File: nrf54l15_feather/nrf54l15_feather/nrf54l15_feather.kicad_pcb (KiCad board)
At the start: 4 copper layers, 66 x 25.4 mm, 63 parts, among them CN1 503480-1400, IC1 AEM10330-QFN, J1 TYPE-C-31-M-12, J3 FTSH-105-01-L-DV-K, U2 nPM1300-QEXX, U4 S2B-PH-K-S-GW, U5 S2B-PH-K-S-GW, U6 nRF54L15-QFXX, X1 XL7EL89CKI-111YLC-32M

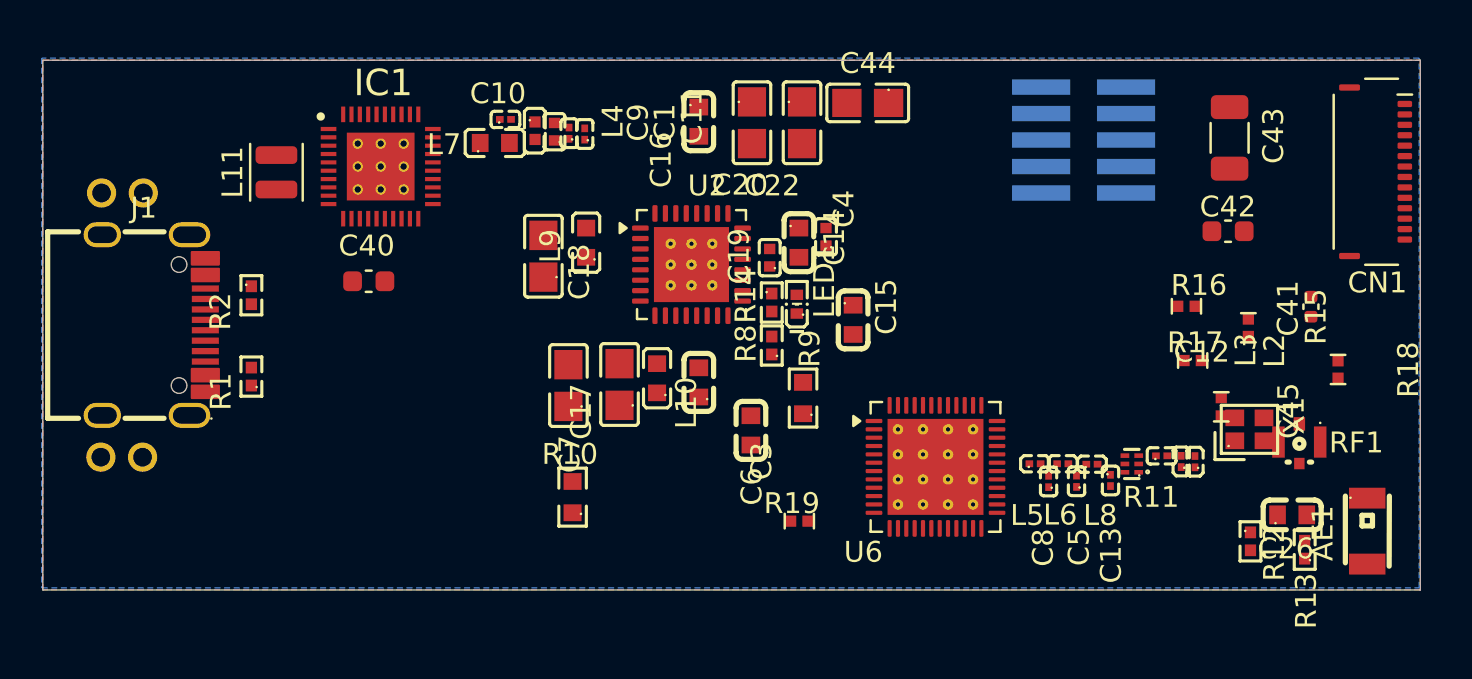
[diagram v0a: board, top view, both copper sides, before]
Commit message: Update the nRF54L15 feather and add the feather sens1 and pouch gateway designs.
Co-authored-by: Cursor <cursoragent@cursor.com>
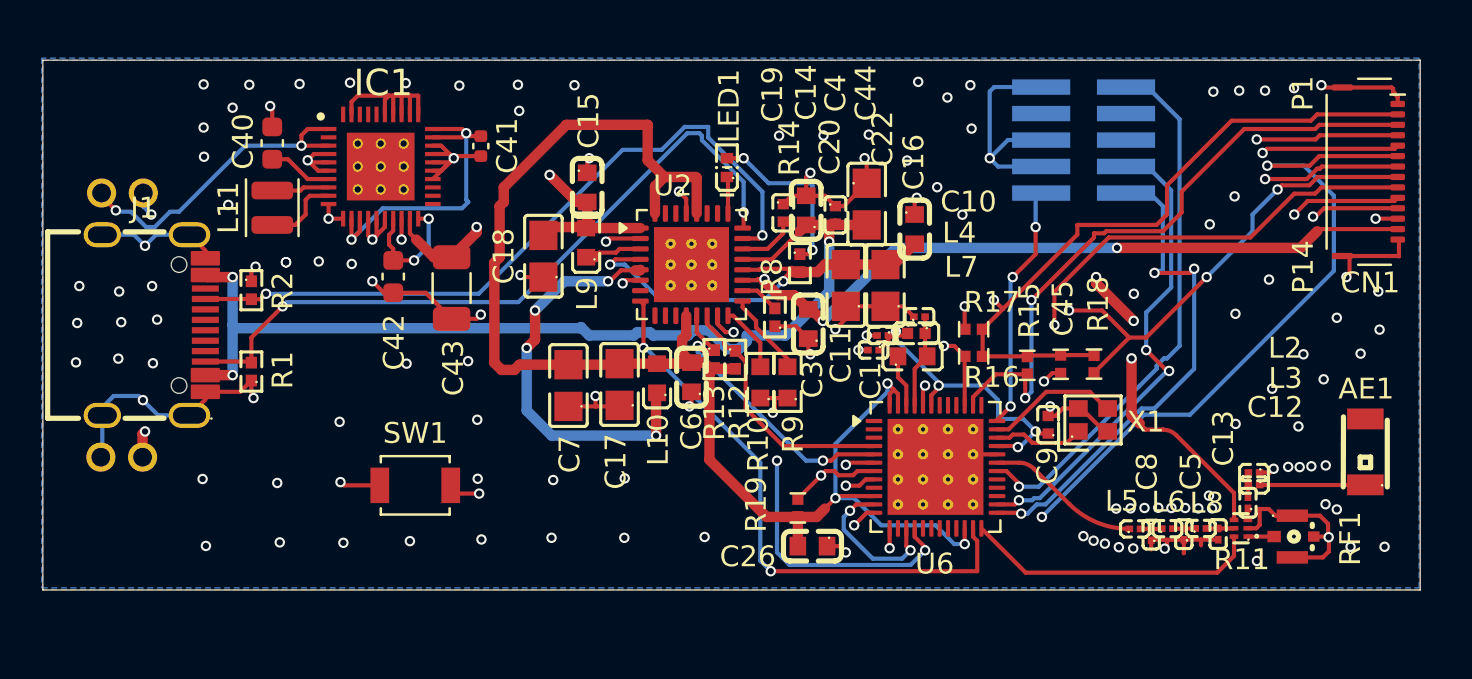
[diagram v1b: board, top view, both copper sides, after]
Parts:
- added SW1: SW_Push, Button_Switch_SMD:SW_SPST_B3U-1000P, F.Cu at (107.9, 130.4)
- moved C41 40.5 mm to (111.0, 114.1)
- moved C42 40.1 mm to (106.8, 120.4), turned to -90 degrees
- moved C43 38.0 mm to (109.6, 120.9), turned to -90 degrees
- moved R13 29.7 mm to (122.2, 124.3), turned to -90 degrees
- moved C9 27.5 mm to (138.2, 127.5)
- moved R12 26.2 mm to (123.2, 124.4)
- moved C26 23.0 mm to (126.9, 133.3), turned to 180 degrees
- moved L7 22.5 mm to (131.7, 124.2)
- moved C10 22.0 mm to (132.0, 122.3)
- moved L4 20.7 mm to (131.9, 123.1), turned to 180 degrees
- moved C1 17.9 mm to (129.8, 123.9), turned to 180 degrees
- moved C11 17.2 mm to (130.3, 123.2), turned to 180 degrees
- moved C15 14.2 mm to (116.1, 116.1)
- moved R18 11.7 mm to (140.4, 124.6), turned to -90 degrees
- moved C16 11.6 mm to (131.8, 118.1)
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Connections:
- U2 pad 15: unconnected-(U2-SHPHLD-Pad15) -> Net-(U2-SHPHLD)
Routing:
- net GND: track 0.00 -> 124.5 mm, vias 0 -> 133
- net VDDIO: track 0.00 -> 89.9 mm, vias 0 -> 6
- net VBAT: track 0.00 -> 76.7 mm, vias 0 -> 5
- net VOUT1: track 0.00 -> 55.0 mm, vias 0 -> 4
- net SENS_CS: track 0.00 -> 53.2 mm, vias 0 -> 5
- net SENS_MISO: track 0.00 -> 52.2 mm, vias 0 -> 3
- net VSENS: track 0.00 -> 51.0 mm, vias 0 -> 2
- net VBUS: track 0.00 -> 48.0 mm, vias 0 -> 3
- net SENS_SCK: track 0.00 -> 45.3 mm, vias 0 -> 2
- net SENS_MOSI: track 0.00 -> 42.3 mm, vias 0 -> 3
- net SENS_INT: track 0.00 -> 41.6 mm, vias 0 -> 3
- net SENS_ID: track 0.00 -> 38.8 mm, vias 0 -> 2
- net CC1: track 0.00 -> 34.8 mm, vias 0 -> 2
- net CC2: track 0.00 -> 34.4 mm, vias 0 -> 2
- net SENS_AIN: track 0.00 -> 33.3 mm, vias 0 -> 2
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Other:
- board text added: "P1"
- board text added: "P14"
